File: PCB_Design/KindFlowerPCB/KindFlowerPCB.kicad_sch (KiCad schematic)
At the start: 13 parts, among them J1 LiPo_Connector, J2 FSR_1, J3 Wireless_Charger, J4 FSR_2, J5 FSR_3, J6 FSR_0, J7 NeopixelStrip1, J8 NeopixelStrip2

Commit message: PCB file updates
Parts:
- added H1: MountingHole, Images:SmFistBmp, symbol Mechanical:MountingHole
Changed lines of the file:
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@@
+    )
+  )
+  (symbol (lib_id "Mechanical:MountingHole") (at 92.71 39.37 0) (unit 1)
+    (in_bom yes) (on_board yes) (dnp no) (fields_autoplaced)
+    (property "Reference" "H1" (at 95.25 38.1 0)
+      (effects (font (size 1.27 1.27)) (justify left))
+    )
+    (property "Value" "MountingHole" (at 95.25 40.64 0)
+      (effects (font (size 1.27 1.27)) (justify left))
+    )
+    (property "Footprint" "Images:SmFistBmp" (at 92.71 39.37 0)
+      (effects (font (size 1.27 1.27)) hide)
+    )
+    (property "Datasheet" "~" (at 92.71 39.37 0)
+      (effects (font (size 1.27 1.27)) hide)
+    )
+    (instances
+      (project "KindFlowerPCB"
+        (path "/6b2a48b2-d72a-4636-9928-5700417c1281"
+          (reference "H1") (unit 1)
+        )
+      )
     )
   )

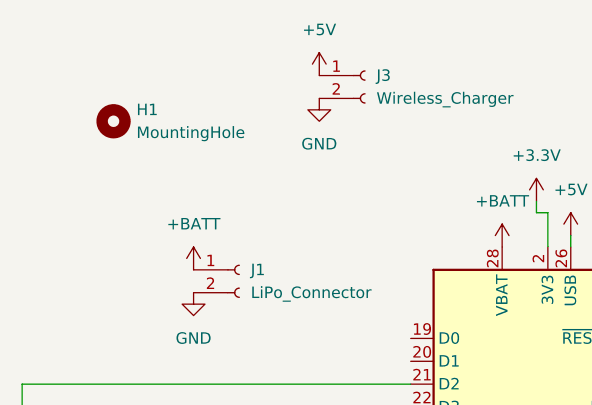
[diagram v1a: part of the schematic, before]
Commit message: Updated KiCad files, redesigned PCB
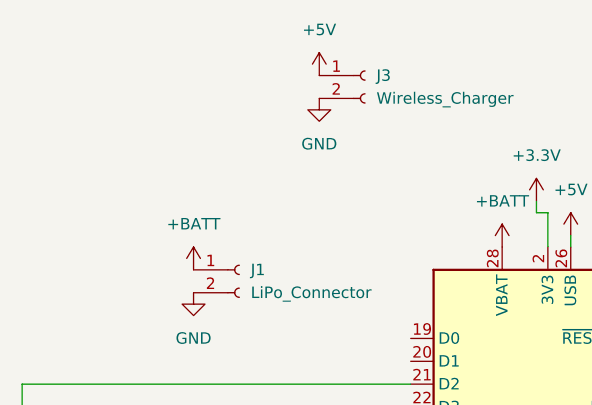
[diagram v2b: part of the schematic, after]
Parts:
- removed H1: MountingHole, Images:SmFistBmp, symbol Mechanical:MountingHole
- A1: footprint Module:Adafruit_Feather_WithMountingHoles -> Module:Adafruit_Feather
- J1: footprint Connector_JST:JST_PH_S2B-PH-K_1x02_P2.00mm_Horizontal -> TerminalBlock_Phoenix:TerminalBlock_Phoenix_MPT-0,5-2-2.54_1x02_P2.54mm_Horizontal
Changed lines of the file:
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@@
       (effects (font (size 1.27 1.27)) (justify left))
     )
-    (property "Footprint" "Module:Adafruit_Feather_WithMountingHoles" (at 140.97 118.11 0)
+    (property "Footprint" "Module:Adafruit_Feather" (at 140.97 118.11 0)
       (effects (font (size 1.27 1.27)) (justify left) hide)
     )
@@
         (path "/6b2a48b2-d72a-4636-9928-5700417c1281"
           (reference "A1") (unit 1)
-        )
-      )
-    )
-  )
-  (symbol (lib_id "Mechanical:MountingHole") (at 92.71 39.37 0) (unit 1)
-    (in_bom yes) (on_board yes) (dnp no) (fields_autoplaced)
-    (property "Reference" "H1" (at 95.25 38.1 0)
-      (effects (font (size 1.27 1.27)) (justify left))
-    )
-    (property "Value" "MountingHole" (at 95.25 40.64 0)
-      (effects (font (size 1.27 1.27)) (justify left))
-    )
-    (property "Footprint" "Images:SmFistBmp" (at 92.71 39.37 0)
-      (effects (font (size 1.27 1.27)) hide)
-    )
-    (property "Datasheet" "~" (at 92.71 39.37 0)
-      (effects (font (size 1.27 1.27)) hide)
-    )
-    (instances
-      (project "KindFlowerPCB"
-        (path "/6b2a48b2-d72a-4636-9928-5700417c1281"
-          (reference "H1") (unit 1)
         )
       )
@@
       (effects (font (size 1.27 1.27)) (justify left))
     )
-    (property "Footprint" "Connector_JST:JST_PH_S2B-PH-K_1x02_P2.00mm_Horizontal" (at 106.68 55.88 0)
+    (property "Footprint" "TerminalBlock_Phoenix:TerminalBlock_Phoenix_MPT-0,5-2-2.54_1x02_P2.54mm_Horizontal" (at 106.68 55.88 0)
       (effects (font (size 1.27 1.27)) hide)
     )

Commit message: Updated PCB files
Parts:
- A1: value Adafruit_Feather_Generic -> Particle_Photon_2; footprint Module:Adafruit_Feather -> ParticleBoards:Photon_2; symbol MCU_Module:Adafruit_Feather_Generic -> ParticlePhoton2:Photon_2
- R2, R3, R4, R5: value R_10k -> R_11k
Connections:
- net at J6.2 (Pin_2), R2.1: now also A1.8 (A5); no longer A1.10 (A5)
- net at J7.2 (Pin_2), J8.2 (Pin_2): now also A1.19 (D2); no longer A1.21 (D2)
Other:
- moved on the sheet: J1
